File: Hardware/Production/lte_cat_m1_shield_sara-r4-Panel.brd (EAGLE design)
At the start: 68.1 x 53.3 mm, 180 parts, among them J8 NANO_SIM, J9 U.FL, Q1 2.5A/30V/105mΩ, Q2 600mA/40V, U1 TXB0104, U2 AP2112K-3.3, U3 MCP73831, U4 AP7361C-33FGE, U5 SARA-R410M-2B

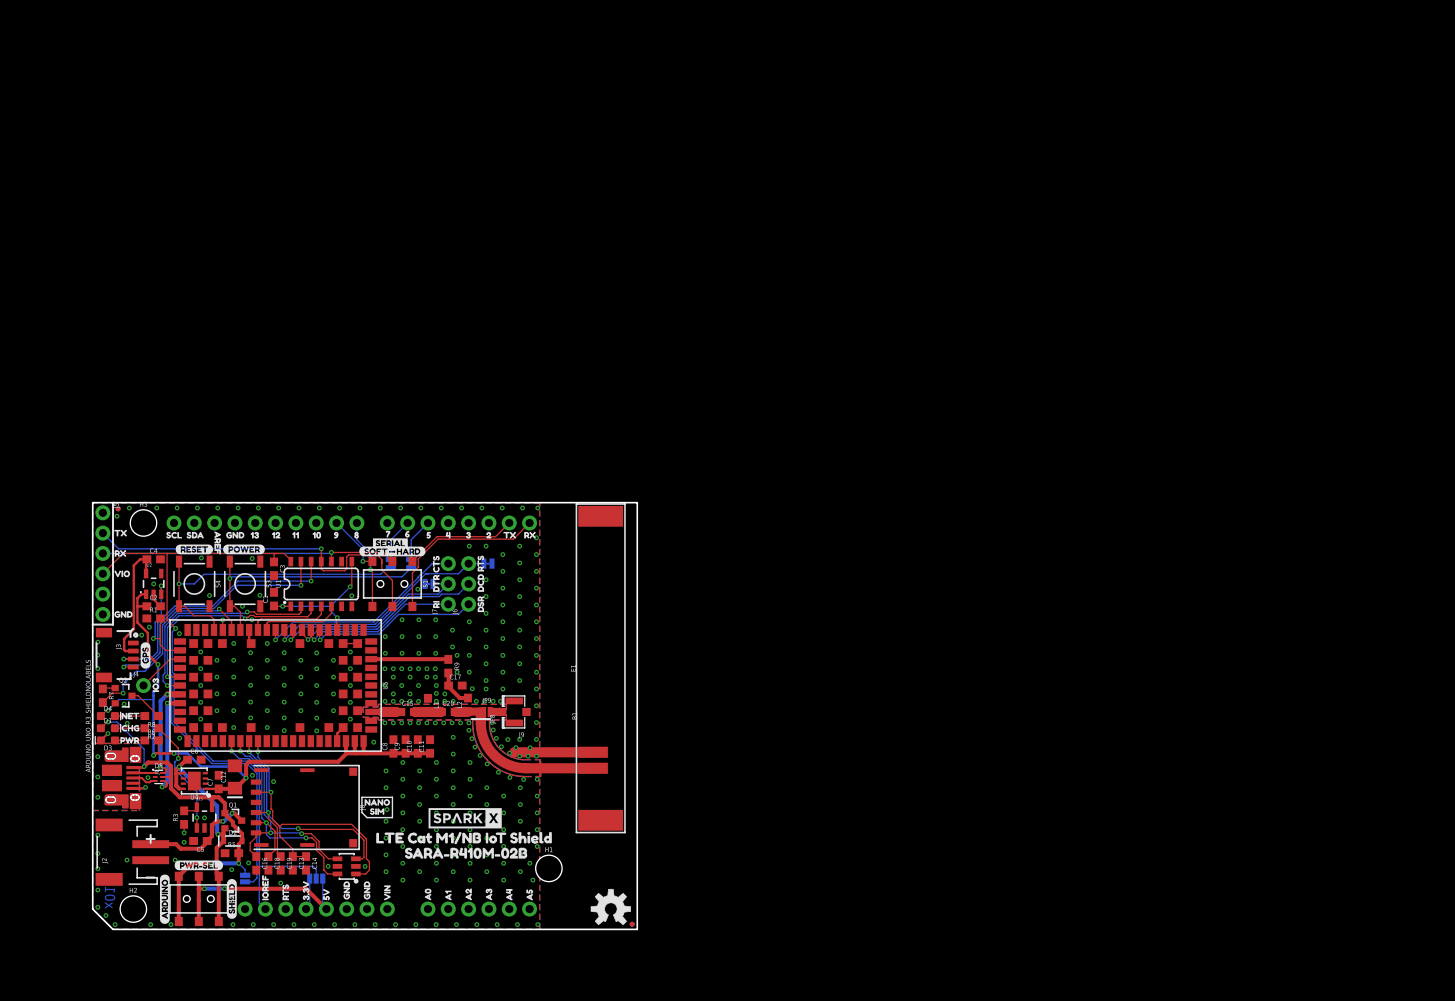
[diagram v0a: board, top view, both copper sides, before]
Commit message: hardware revisions post u-blox review - x02 production hardware
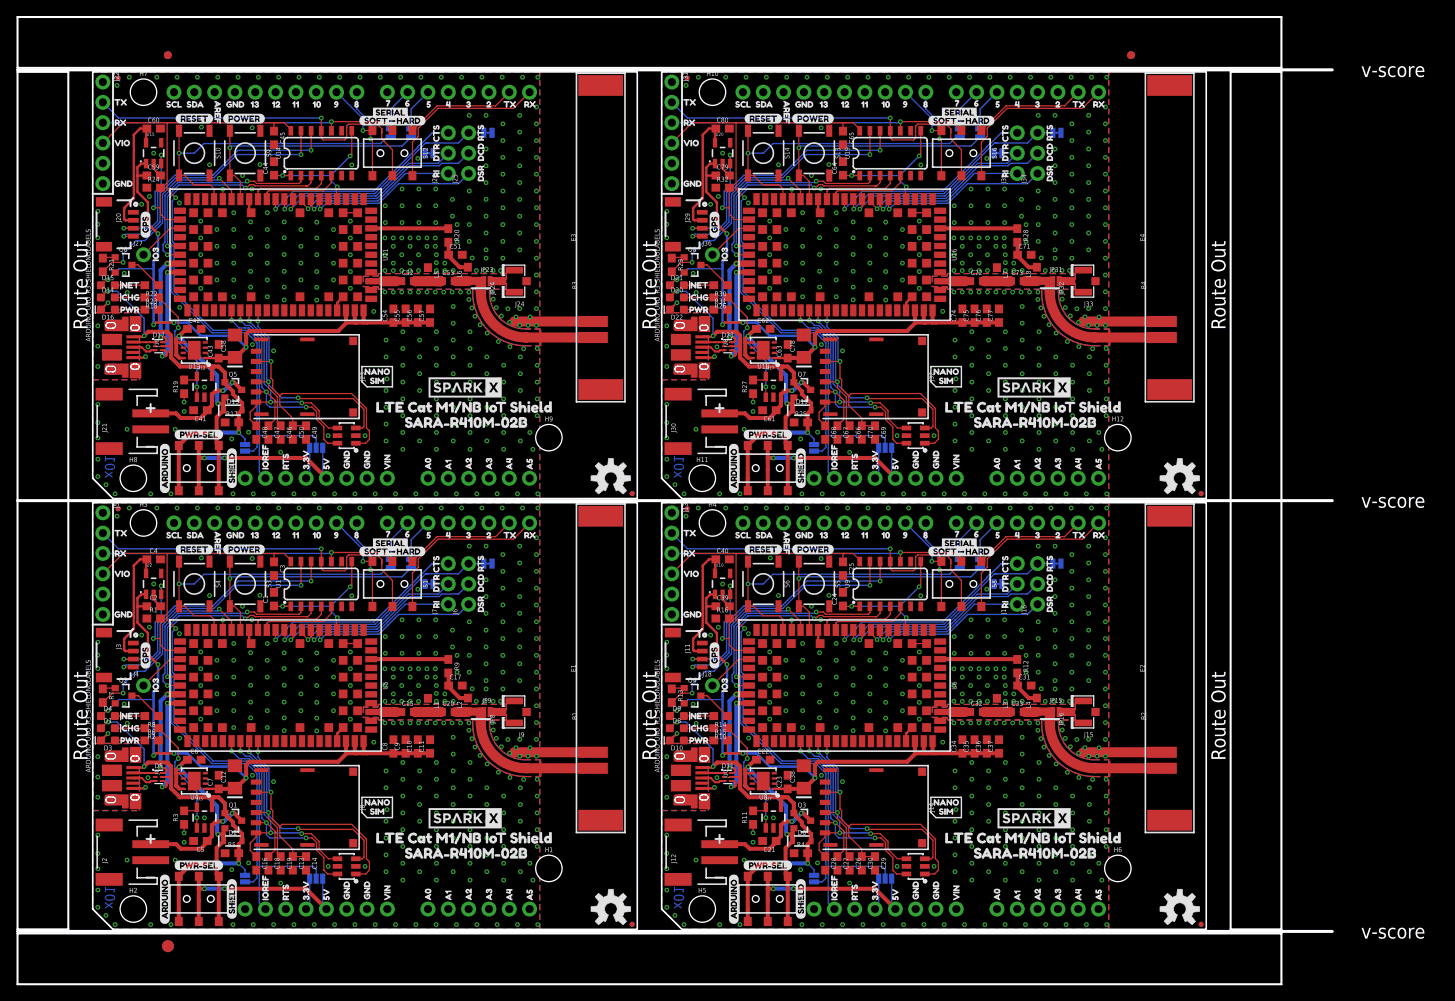
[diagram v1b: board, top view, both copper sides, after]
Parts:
- removed FRAME1, FRAME2: FRAME-LETTER, SparkFun-Aesthetics:CREATIVE_COMMONS
- added B2, B3, B4: ARDUINO_UNO_R3_SHIELDNOLABELS, SparkFun-Boards:UNO_R3_SHIELD_NOLABELS
- added C21, C22, C23, C41, C42, C43, C61, C62, C63: 4.7uF, SparkFun-Capacitors:0603
- added C24, C25, C30, C34, C44, C45, C50, C54, C64, C65, C70, C74: 0.1uF, SparkFun-Capacitors:0603
- added C26, C27, C28, C29, C46, C47, C48, C49, C66, C67, C68, C69: 47pF, SparkFun-Capacitors:0603
- added C31, C51, C71: 27pF, SparkFun-Capacitors:0603
- added C32, C36, C52, C56, C72, C76: 15pF, SparkFun-Capacitors:0603
- added C33, C53, C73: 33pF, SparkFun-Capacitors:0603
- added C35, C55, C75: 10nF, SparkFun-Capacitors:0603
- added C37, C57, C77: 68pF, ublox:0603
- added C38, C58, C78: 100uF, ublox:1206-POLAR
- added C39, C40, C59, C60, C79, C80: 1.0uF, SparkFun-Capacitors:0603
- added D10, D16, D22: RED, SparkFun-LED:LED-0603
- added D11, D17, D23: PRTR5V0U2F, ublox:SOT886
- added D12, D18, D24: DT1042-04SO-7, ublox:SOT23-6L
- added D13, D19, D6: 1A/23V/620mV, SparkFun-DiscreteSemi:SOD-323
- added D14, D20, D8: Yellow, SparkFun-LED:LED-0603
- added D15, D21, D9: BLUE, SparkFun-LED:LED-0603
- added E$1, E$2, E$3, E$4: (no value), SparkFun-Aesthetics:FIDUCIAL-1X2
- added E$5, E$6: (no value), SparkFun-Retired:FIDUCIAL-1.5X3
- added E2, E3, E4: MOLEX-146200, ublox:MOLEX_146200
- added FD10, FD11, FD12, FD13, FD14, FD15, FD16, FD5, FD6, FD7, FD8, FD9: FIDUCIALUFIDUCIAL, SparkFun-Aesthetics:FIDUCIAL-MICRO
- added H10, H11, H12, H4, H5, H6, H7, H8, H9: STAND-OFF, SparkFun-Hardware:STAND-OFF
- added J10, J19, J28: (no value), SparkFun-Connectors:USB-MICROB-PTH-MILL
- added J11, J20, J29: (no value), SparkFun-Connectors:1X04_1MM_RA
- added J12, J21, J30: (no value), SparkFun-Connectors:JST-2-SMD
- added J13, J22, J31: (no value), SparkFun-Connectors:1X06_NO_SILK
- added J14, J23, J32: NANO_SIM, ublox:NANO_SIM_WURTH_693043020611
- added J15, J24, J33: U.FL, SparkFun-Connectors:U.FL
- added J16, J17, J25, J26, J34, J35: (no value), SparkFun-Connectors:1X03_NO_SILK
- added J18, J27, J36: (no value), SparkFun-Connectors:1X01_NO_SILK
- added JP1, JP17, JP25: VUSB_DET, SparkFun-Jumpers:SMT-JUMPER_2_NO_SILK
- added JP10, JP11, JP18, JP19, JP26, JP27: JUMPER-SMT_2_NC_TRACE_SILK, SparkFun-Jumpers:SMT-JUMPER_2_NC_TRACE_SILK
- added JP12, JP20, JP28: IOREF-SEL, SparkFun-Jumpers:SMT-JUMPER_3_NO_SILK
- added JP13, JP14, JP21, JP22, JP29, JP30: (no value), SparkFun-Jumpers:SMT-JUMPER_2_NC_TRACE_SILK
- added JP15, JP23, JP31: J-U.FL, SparkFun-Jumpers:SMT-JUMPER_2_NO_NO-SILK
- added JP16, JP24, JP32: J-CHIP, SparkFun-Jumpers:SMT-JUMPER_2_NC_TRACE_NO-SILK
- added L3, L5, L7: 39nH, ublox:0603
- added L4, L6, L8: 68nH, ublox:0603
- added LOGO3, LOGO5, LOGO7: SPARKX-LOGO4, SparkX:SPARKX-MEDIUM
- added LOGO4, LOGO6, LOGO8: OSHW-LOGOM, SparkFun-Aesthetics:OSHW-LOGO-M
- added Q3, Q5, Q7: 2.5A/30V/105mΩ, SparkFun-DiscreteSemi:SOT23-3
- added Q4, Q6, Q8: 600mA/40V, SparkFun-DiscreteSemi:SOT23-3
- added R10, R14, R15, R18, R22, R23, R26, R30, R31: 1k, SparkFun-Resistors:0603
- added R11, R19, R27: 2.0k, SparkFun-Resistors:0603
- added R12, R13, R17, R20, R21, R25, R28, R29, R4: 10k, SparkFun-Resistors:0603
- added R16, R24, R32: 47k, SparkFun-Resistors:0603
- added S10, S14, S6: RESET, SparkFun-Switches:TACTILE_SWITCH_SMD_5.2MM
- added S11, S12, S15, S16, S7, S8: (no value), SparkFun-Switches:SWITCH_DPDT_SMD_AYZ0202
- added S13, S5, S9: PWR_ON, SparkFun-Switches:TACTILE_SWITCH_SMD_5.2MM
- added U$103, U$177, U$208, U$280, U$311, U$383: (no value), buzzard_labels:SDA1
- added U$106, U$179, U$209, U$282, U$312, U$385: (no value), buzzard_labels:AREF2
- added U$107, U$139, U$140, U$167, U$168, U$181, U$195, U$196, U$210, U$242, U$243, U$270, U$271, U$284, U$298, U$299, U$313, U$345, U$346, U$373, U$374, U$387, U$401, U$402: (no value), buzzard_labels:GND3
- added U$108, U$180, U$211, U$283, U$314, U$386: (no value), buzzard_labels:134
- added U$109, U$182, U$212, U$285, U$315, U$388: (no value), buzzard_labels:125
- added U$110, U$183, U$213, U$286, U$316, U$389: (no value), buzzard_labels:116
- added U$111, U$184, U$214, U$287, U$317, U$390: (no value), buzzard_labels:107
- added U$112, U$185, U$215, U$288, U$318, U$391: (no value), buzzard_labels:98
- added U$113, U$186, U$216, U$289, U$319, U$392: (no value), buzzard_labels:89
- added U$114, U$187, U$217, U$290, U$320, U$393: (no value), buzzard_labels:714
- added U$115, U$156, U$188, U$218, U$259, U$291, U$321, U$362, U$394: (no value), buzzard_labels:615
- added U$116, U$155, U$189, U$219, U$258, U$292, U$322, U$361, U$395: (no value), buzzard_labels:516
- added U$117, U$190, U$220, U$293, U$323, U$396: (no value), buzzard_labels:417
- added U$118, U$191, U$221, U$294, U$324, U$397: (no value), buzzard_labels:318
- added U$119, U$192, U$222, U$295, U$325, U$398: (no value), buzzard_labels:219
- added U$120, U$129, U$175, U$194, U$223, U$232, U$278, U$297, U$326, U$335, U$381, U$400: (no value), buzzard_labels:RX22
- added U$121, U$130, U$174, U$193, U$224, U$233, U$277, U$296, U$327, U$336, U$380, U$399: (no value), buzzard_labels:TX21
- added U$122, U$225, U$328: (no value), buzzard_labels:CTS23
- added U$123, U$157, U$226, U$260, U$329, U$363: (no value), buzzard_labels:DTR24
- added U$124, U$227, U$330: (no value), buzzard_labels:RI25
- added U$125, U$228, U$331: (no value), buzzard_labels:DSR26
- added U$126, U$229, U$332: (no value), buzzard_labels:DCD27
- added U$127, U$136, U$158, U$171, U$230, U$239, U$261, U$274, U$333, U$342, U$364, U$377: (no value), buzzard_labels:RTS28
- added U$128, U$176, U$231, U$279, U$334, U$382: (no value), buzzard_labels:VIO29
- added U$131, U$173, U$234, U$276, U$337, U$379: (no value), buzzard_labels:IO334
- added U$132, U$235, U$338: (no value), buzzard_labels:NET31
- added U$133, U$236, U$339: (no value), buzzard_labels:CHG33
- added U$134, U$153, U$237, U$256, U$340, U$359: (no value), buzzard_labels:PWR32
- added U$135, U$150, U$172, U$238, U$253, U$275, U$341, U$356, U$378: (no value), buzzard_labels:IOREF39
- added U$137, U$152, U$170, U$240, U$255, U$273, U$343, U$358, U$376: (no value), buzzard_labels:3#3V41
- added U$138, U$151, U$169, U$241, U$254, U$272, U$344, U$357, U$375: (no value), buzzard_labels:5V42
- added U$141, U$166, U$244, U$269, U$347, U$372: (no value), buzzard_labels:VIN43
- added U$142, U$165, U$245, U$268, U$348, U$371: (no value), buzzard_labels:A044
- added U$143, U$164, U$246, U$267, U$349, U$370: (no value), buzzard_labels:A145
- added U$144, U$163, U$247, U$266, U$350, U$369: (no value), buzzard_labels:A246
- added U$145, U$162, U$248, U$265, U$351, U$368: (no value), buzzard_labels:A347
- added U$146, U$161, U$249, U$264, U$352, U$367: (no value), buzzard_labels:A448
- added U$147, U$160, U$250, U$263, U$353, U$366: (no value), buzzard_labels:A549
- added U$148, U$251, U$354: (no value), buzzard_labels:NANO50
- added U$149, U$252, U$355: (no value), buzzard_labels:SIM51
- added U$154, U$257, U$360: (no value), buzzard_labels:RST40
- added U$159, U$262, U$365: (no value), buzzard_labels:VUSB_DET52
- added U$178, U$207, U$281, U$310, U$384, U$40: (no value), buzzard_labels:SCL0
- added U$197, U$300, U$403: (no value), buzzard_labels:LTE_CAT_M1#NB_IOT_SHIELD55
- added U$198, U$301, U$404: (no value), buzzard_labels:SARA#R410M#02B54
- added U$199, U$302, U$405: (no value), buzzard_labels:SOFT#HARD50
- added U$200, U$303, U$406: (no value), buzzard_labels:SERIAL57
- added U$201, U$304, U$407: (no value), buzzard_labels:POWER49
- added U$202, U$305, U$408: (no value), buzzard_labels:RESET48
- added U$203, U$306, U$409: (no value), buzzard_labels:GPS47
- added U$204, U$307, U$410: (no value), buzzard_labels:ARDUINO51
- added U$205, U$308, U$411: (no value), buzzard_labels:SHIELD52
- added U$206, U$309, U$412: (no value), buzzard_labels:PWR#SEL53
- added U10, U15, U20: AP2112K-3.3, SparkFun-IC-Power:SOT23-5
- added U11, U16, U6: SARA-R410M-2B, ublox:SARA-LGA
- added U12, U17, U7: MCP73831, SparkFun-PowerIC:SOT23-5
- added U13, U18, U8: AP7361C-33FGE, ublox:8-UDFN
- added U14, U19, U9: TXB0104, SparkFun-IC-Comms:SO14
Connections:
- new net 1.8V1: C24.1, U6.4, U9.1, U9.8
- new net 1.8V2: C44.1, U11.4, U14.1, U14.8
- new net 1.8V3: C64.1, U16.4, U19.1, U19.8
- new net 3.3V1: C23.1, C34.1, C35.1, C36.1, C37.1, C38.1, C39.1, D9.A, R15.2, U10.1, U6.51, U6.52, U6.53, U8.1
- new net 3.3V2: C43.1, C54.1, C55.1, C56.1, C57.1, C58.1, C59.1, D15.A, R23.2, U11.51, U11.52, U11.53, U13.1, U15.1
- new net 3.3V3: C63.1, C74.1, C75.1, C76.1, C77.1, C78.1, C79.1, D21.A, R31.2, U16.51, U16.52, U16.53, U18.1, U20.1
- new net ANT1: C32.1, U6.56
- new net ANT2: C52.1, U11.56
- new net ANT3: C72.1, U16.56
- new net ANT_DET1: R12.1, U6.62
- new net ANT_DET2: R20.1, U11.62
- new net ANT_DET3: R28.1, U16.62
- new net ARDUINO-3.3V1: B2.3.3V, JP12.3
- new net ARDUINO-3.3V2: B3.3.3V, JP20.3
- new net ARDUINO-3.3V3: B4.3.3V, JP28.3
- new net ARDUINO-5V1: B2.5V, JP12.1, S7.2, S7.5
- new net ARDUINO-5V2: B3.5V, JP20.1, S11.2, S11.5
- new net ARDUINO-5V3: B4.5V, JP28.1, S15.2, S15.5
- new net CTS1: J17.3, U6.11
- new net CTS2: J26.3, U11.11
- new net CTS3: J35.3, U16.11
- new net D+1: D11.6, U6.28
- new net D+2: D17.6, U11.28
- new net D+3: D23.6, U16.28
- new net D-1: D11.4, U6.29
- new net D-2: D17.4, U11.29
- new net D-3: D23.4, U16.29
- new net DCD1: J16.2, U6.8
- new net DCD2: J25.2, U11.8
- new net DCD3: J34.2, U16.8
- new net DSR1: J16.1, U6.6
- new net DSR2: J25.1, U11.6
- new net DSR3: J34.1, U16.6
- new net DTR1: J17.2, JP13.2, U6.9
- new net DTR2: J26.2, JP21.2, U11.9
- new net DTR3: J35.2, JP29.2, U16.9
- new net GND1: B2.AREF, B2.GND@0, B2.GND@1, B2.GND@2, C21.2, C22.2, C23.2, C24.2, C25.2, C26.2, C27.2, C28.2, C29.2, C30.2, C31.2, C34.2, C35.2, C36.2, C37.2, C38.2, C39.2, C40.2, D10.C, D11.2, D12.2, D12.5, E2.GND, J10.GND, J11.1, J12.1, J13.6, J14.C5, J15.1, J15.2, JP13.1, JP14.1, L3.1, Q4.2, R11.1, R16.1, R4.1, S5.1, S5.2, S6.1, S6.2, U10.2, U6.1, U6.14, U6.20, U6.21, U6.22, U6.3, U6.30, U6.32, U6.33, U6.43, U6.5, U6.50, U6.54, U6.55, U6.57, U6.58, U6.59, U6.60, U6.61, U6.63, U6.64, U6.65, U6.66, U6.67, U6.68, U6.69, U6.70, U6.71, U6.72, U6.73, U6.74, U6.75, U6.76, U6.77, U6.78, U6.79, U6.80, U6.81, U6.82, U6.83, U6.84, U6.85, U6.86, U6.87, U6.88, U6.89, U6.90, U6.91, U6.92, U6.93, U6.94, U6.95, U6.96, U7.2, U8.4, U8.EP, U9.7
- new net GND2: B3.AREF, B3.GND@0, B3.GND@1, B3.GND@2, C41.2, C42.2, C43.2, C44.2, C45.2, C46.2, C47.2, C48.2, C49.2, C50.2, C51.2, C54.2, C55.2, C56.2, C57.2, C58.2, C59.2, C60.2, D16.C, D17.2, D18.2, D18.5, E3.GND, J19.GND, J20.1, J21.1, J22.6, J23.C5, J24.1, J24.2, JP21.1, JP22.1, L5.1, Q6.2, R17.1, R19.1, R24.1, S10.1, S10.2, S9.1, S9.2, U11.1, U11.14, U11.20, U11.21, U11.22, U11.3, U11.30, U11.32, U11.33, U11.43, U11.5, U11.50, U11.54, U11.55, U11.57, U11.58, U11.59, U11.60, U11.61, U11.63, U11.64, U11.65, U11.66, U11.67, U11.68, U11.69, U11.70, U11.71, U11.72, U11.73, U11.74, U11.75, U11.76, U11.77, U11.78, U11.79, U11.80, U11.81, U11.82, U11.83, U11.84, U11.85, U11.86, U11.87, U11.88, U11.89, U11.90, U11.91, U11.92, U11.93, U11.94, U11.95, U11.96, U12.2, U13.4, U13.EP, U14.7, U15.2
- new net GND3: B4.AREF, B4.GND@0, B4.GND@1, B4.GND@2, C61.2, C62.2, C63.2, C64.2, C65.2, C66.2, C67.2, C68.2, C69.2, C70.2, C71.2, C74.2, C75.2, C76.2, C77.2, C78.2, C79.2, C80.2, D22.C, D23.2, D24.2, D24.5, E4.GND, J28.GND, J29.1, J30.1, J31.6, J32.C5, J33.1, J33.2, JP29.1, JP30.1, L7.1, Q8.2, R25.1, R27.1, R32.1, S13.1, S13.2, S14.1, S14.2, U16.1, U16.14, U16.20, U16.21, U16.22, U16.3, U16.30, U16.32, U16.33, U16.43, U16.5, U16.50, U16.54, U16.55, U16.57, U16.58, U16.59, U16.60, U16.61, U16.63, U16.64, U16.65, U16.66, U16.67, U16.68, U16.69, U16.70, U16.71, U16.72, U16.73, U16.74, U16.75, U16.76, U16.77, U16.78, U16.79, U16.80, U16.81, U16.82, U16.83, U16.84, U16.85, U16.86, U16.87, U16.88, U16.89, U16.90, U16.91, U16.92, U16.93, U16.94, U16.95, U16.96, U17.2, U18.4, U18.EP, U19.7, U20.2
- new net GPIO10: R29.2, U16.16
- new net GPIO11: R32.2, U16.23, U20.3
- new net GPIO12: J36.1, U16.24
- new net GPIO4: R13.2, U6.16
- new net GPIO5: R16.2, U10.3, U6.23
- new net GPIO6: J18.1, U6.24
- new net GPIO7: R21.2, U11.16
- new net GPIO8: R24.2, U11.23, U15.3
- new net GPIO9: J27.1, U11.24
- new net GPS-3.3V1: C40.1, J11.2, U10.5
- new net GPS-3.3V2: C60.1, J20.2, U15.5
- new net GPS-3.3V3: C80.1, J29.2, U20.5
- new net HARDRX-ARDUINO1: B2.RX, S8.1
- new net HARDRX-ARDUINO2: B3.RX, S12.1
- new net HARDRX-ARDUINO3: B4.RX, S16.1
- new net HARDTX-ARDUINO1: B2.TX, S8.4
- new net HARDTX-ARDUINO2: B3.TX, S12.4
- new net HARDTX-ARDUINO3: B4.TX, S16.4
- new net IOREF1: B2.IOREF, C25.1, J13.4, JP12.2, U9.14
- new net IOREF2: B3.IOREF, C45.1, J22.4, JP20.2, U14.14
- new net IOREF3: B4.IOREF, C65.1, J31.4, JP28.2, U19.14
- new net N$2: D8.C, R10.2
- new net N$23: J15.FEED, JP15.2
- new net N$24: Q4.1, R13.1
- new net N$25: D10.A, R15.1
- new net N$26: D9.C, R14.2
- new net N$27: Q4.3, R14.1
- new net N$28: B2.D5, JP11.1
- new net N$29: B2.D6, JP10.1
- new net N$3: R10.1, U7.1
- new net N$30: C33.2, JP15.1, JP16.1, L4.1
- new net N$31: E2.FEED, JP16.2
- new net N$33: D11.1, J10.D-
- new net N$34: D11.3, J10.D+
- new net N$35: D14.C, R18.2
- new net N$36: R18.1, U12.1
- new net N$37: R19.2, U12.5
- new net N$38: C51.1, L6.2, R20.2
- new net N$39: C52.2, C53.1, L5.2
- new net N$4: R11.2, U7.5
- new net N$40: J24.FEED, JP23.2
- new net N$41: Q6.1, R21.1
- new net N$42: D16.A, R23.1
- new net N$43: D15.C, R22.2
- new net N$44: Q6.3, R22.1
- new net N$45: B3.D5, JP19.1
- new net N$46: B3.D6, JP18.1
- new net N$47: C53.2, JP23.1, JP24.1, L6.1
- new net N$48: E3.FEED, JP24.2
- new net N$5: C31.1, L4.2, R12.2
- new net N$50: D17.1, J19.D-
- new net N$51: D17.3, J19.D+
- new net N$52: D20.C, R26.2
- new net N$53: R26.1, U17.1
- new net N$54: R27.2, U17.5
- new net N$55: C71.1, L8.2, R28.2
- new net N$56: C72.2, C73.1, L7.2
- new net N$57: J33.FEED, JP31.2
- new net N$58: Q8.1, R29.1
- new net N$59: D22.A, R31.1
- new net N$6: C32.2, C33.1, L3.2
- new net N$60: D21.C, R30.2
- new net N$61: Q8.3, R30.1
- new net N$62: B4.D5, JP27.1
- new net N$63: B4.D6, JP26.1
- new net N$64: C73.2, JP31.1, JP32.1, L8.1
- new net N$65: E4.FEED, JP32.2
- new net N$67: D23.1, J28.D-
- new net N$68: D23.3, J28.D+
- new net PWR_ON1: JP11.2, S5.3, S5.4, U6.15
- new net PWR_ON2: JP19.2, S9.3, S9.4, U11.15
- new net PWR_ON3: JP27.2, S13.3, S13.4, U16.15
- new net RESET_N1: JP10.2, S6.3, S6.4, U6.18
- new net RESET_N2: JP18.2, S10.3, S10.4, U11.18
- new net RESET_N3: JP26.2, S14.3, S14.4, U16.18
- new net RI1: J17.1, U6.7
- new net RI2: J26.1, U11.7
- new net RI3: J35.1, U16.7
- new net RTS1: J16.3, JP14.2, U6.10
- new net RTS2: J25.3, JP22.2, U11.10
- new net RTS3: J34.3, JP30.2, U16.10
- new net RX-ARDUINO1: J13.2, S8.2, U9.11
- new net RX-ARDUINO2: J22.2, S12.2, U14.11
- new net RX-ARDUINO3: J31.2, S16.2, U19.11
- new net RX-CELL1: U6.12, U9.5
- new net RX-CELL2: U11.12, U14.5
- new net RX-CELL3: U16.12, U19.5
- new net SCL-CELL1: U6.27, U9.2
- new net SCL-CELL2: U11.27, U14.2
- new net SCL-CELL3: U16.27, U19.2
- new net SCL-QWIIC1: J11.4, U9.13
- new net SCL-QWIIC2: J20.4, U14.13
- new net SCL-QWIIC3: J29.4, U19.13
- new net SDA-CELL1: U6.26, U9.3
- new net SDA-CELL2: U11.26, U14.3
- new net SDA-CELL3: U16.26, U19.3
- new net SDA-QWIIC1: J11.3, U9.12
- new net SDA-QWIIC2: J20.3, U14.12
- new net SDA-QWIIC3: J29.3, U19.12
- new net SHIELD1: J10.SHIELD, J10.SHIELD10, J10.SHIELD2, J10.SHIELD3, J10.SHIELD4, J10.SHIELD5, J10.SHIELD6, J10.SHIELD7, J10.SHIELD8, J10.SHIELD9
- new net SHIELD2: J19.SHIELD, J19.SHIELD10, J19.SHIELD2, J19.SHIELD3, J19.SHIELD4, J19.SHIELD5, J19.SHIELD6, J19.SHIELD7, J19.SHIELD8, J19.SHIELD9
- new net SHIELD3: J28.SHIELD, J28.SHIELD10, J28.SHIELD2, J28.SHIELD3, J28.SHIELD4, J28.SHIELD5, J28.SHIELD6, J28.SHIELD7, J28.SHIELD8, J28.SHIELD9
- new net SIM_CLK1: C27.1, D12.6, J14.C3, U6.38
- new net SIM_CLK2: C47.1, D18.6, J23.C3, U11.38
- new net SIM_CLK3: C67.1, D24.6, J32.C3, U16.38
- new net SIM_IO1: C28.1, D12.4, J14.C7, U6.39
- new net SIM_IO2: C48.1, D18.4, J23.C7, U11.39
- new net SIM_IO3: C68.1, D24.4, J32.C7, U16.39
- new net SIM_RST1: C26.1, D12.3, J14.C2, U6.40
- new net SIM_RST2: C46.1, D18.3, J23.C2, U11.40
- new net SIM_RST3: C66.1, D24.3, J32.C2, U16.40
- new net SOFTRX-ARDUINO1: B2.D8, S8.3
- new net SOFTRX-ARDUINO2: B3.D8, S12.3
- new net SOFTRX-ARDUINO3: B4.D8, S16.3
- new net SOFTTX-ARDUINO1: B2.D9, S8.6
- new net SOFTTX-ARDUINO2: B3.D9, S12.6
- new net SOFTTX-ARDUINO3: B4.D9, S16.6
- new net TX-ARDUINO1: J13.3, S8.5, U9.10
- new net TX-ARDUINO2: J22.3, S12.5, U14.10
- new net TX-ARDUINO3: J31.3, S16.5, U19.10
- new net TX-CELL1: U6.13, U9.4
- new net TX-CELL2: U11.13, U14.4
- new net TX-CELL3: U16.13, U19.4
- new net VIN1: C22.1, D6.C, Q3.2, S7.1, S7.4, U8.5, U8.8
- new net VIN2: C42.1, D13.C, Q5.2, S11.1, S11.4, U13.5, U13.8
- new net VIN3: C62.1, D19.C, Q7.2, S15.1, S15.4, U18.5, U18.8
- new net VSIM1: C29.1, C30.1, D12.1, J14.C1, U6.41
- new net VSIM2: C49.1, C50.1, D18.1, J23.C1, U11.41
- new net VSIM3: C69.1, C70.1, D24.1, J32.C1, U16.41
- new net VUSB_DET1: JP1.2, U6.17
- new net VUSB_DET2: JP17.2, U11.17
- new net VUSB_DET3: JP25.2, U16.17
- new net V_BATT1: C21.1, J12.2, Q3.3, U7.3
- new net V_BATT2: C41.1, J21.2, Q5.3, U12.3
- new net V_BATT3: C61.1, J30.2, Q7.3, U17.3
- new net V_USB1: D11.5, D6.A, D8.A, J10.VBUS, JP1.1, Q3.1, R4.2, S7.3, S7.6, U7.4
- new net V_USB2: D13.A, D14.A, D17.5, J19.VBUS, JP17.1, Q5.1, R17.2, S11.3, S11.6, U12.4
- new net V_USB3: D19.A, D20.A, D23.5, J28.VBUS, JP25.1, Q7.1, R25.2, S15.3, S15.6, U17.4
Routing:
- net IOREF1: track 0.00 -> 87.7 mm, vias 0 -> 1
- net IOREF3: track 0.00 -> 87.7 mm, vias 0 -> 1
- net IOREF2: track 0.00 -> 87.7 mm, vias 0 -> 1
- net 3.3V1: track 0.00 -> 82.8 mm, vias 0 -> 5
- net 3.3V3: track 0.00 -> 82.8 mm, vias 0 -> 5
- net 3.3V2: track 0.00 -> 82.8 mm, vias 0 -> 5
- net V_USB2: track 0.00 -> 51.6 mm, vias 0 -> 4
- net V_USB3: track 0.00 -> 51.6 mm, vias 0 -> 4
- net V_USB1: track 0.00 -> 51.6 mm, vias 0 -> 4
- net VUSB_DET1: track 0.00 -> 48.2 mm, vias 0 -> 1
- net VUSB_DET2: track 0.00 -> 48.2 mm, vias 0 -> 1
- net VUSB_DET3: track 0.00 -> 48.2 mm, vias 0 -> 1
- net RX-ARDUINO1: track 0.00 -> 47.1 mm, vias 0 -> 1
- net RX-ARDUINO2: track 0.00 -> 47.1 mm, vias 0 -> 1
- net RX-ARDUINO3: track 0.00 -> 47.1 mm, vias 0 -> 1
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- added copper zone on layer 1, net GND1
- added copper zone on layer 16, net GND1
- added copper zone on layer 1, net GND2
- added copper zone on layer 16, net GND2
- added copper zone on layer 1, net GND3
- added copper zone on layer 16, net GND3
- added copper zone on layer 1, net SHIELD1
- added copper zone on layer 16, net SHIELD1
- added copper zone on layer 1, net SHIELD2
- added copper zone on layer 16, net SHIELD2
- added copper zone on layer 1, net SHIELD3
- added copper zone on layer 16, net SHIELD3
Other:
- board size 68.1 x 53.3 mm -> 164.3 x 120.9 mm
- board text added: "Route Out"
- board text added: "v-score"
- board text removed: "Jim Lindblom"
